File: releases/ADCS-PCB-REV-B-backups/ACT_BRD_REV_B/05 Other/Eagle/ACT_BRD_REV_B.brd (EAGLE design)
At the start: 91 x 91 mm, 228 parts, among them J11 TE_1-84953-1, J2 TE_1-84953-1, J4 TE_1-84953-1, J5 830-10-003-20-005000, U1 SIP2100DY-T1-GE3, U10 LM2917MX/NOPB, U12 TSV991AILT, U13 LM2917MX/NOPB, U14 ADS7841E_2K5, U16 DRV10970_MOTOR_DRIVERDRV10970, U17 LM2917MX/NOPB, U19 TSV991AILT, U2 SIP2100DY-T1-GE3, U20 ADS7841E_2K5, U3 SIP2100DY-T1-GE3, U6 DRV10970_MOTOR_DRIVERDRV10970, U7 DRV10970_MOTOR_DRIVERDRV10970, U8 TSV991AILT, U9 ADS7841E_2K5

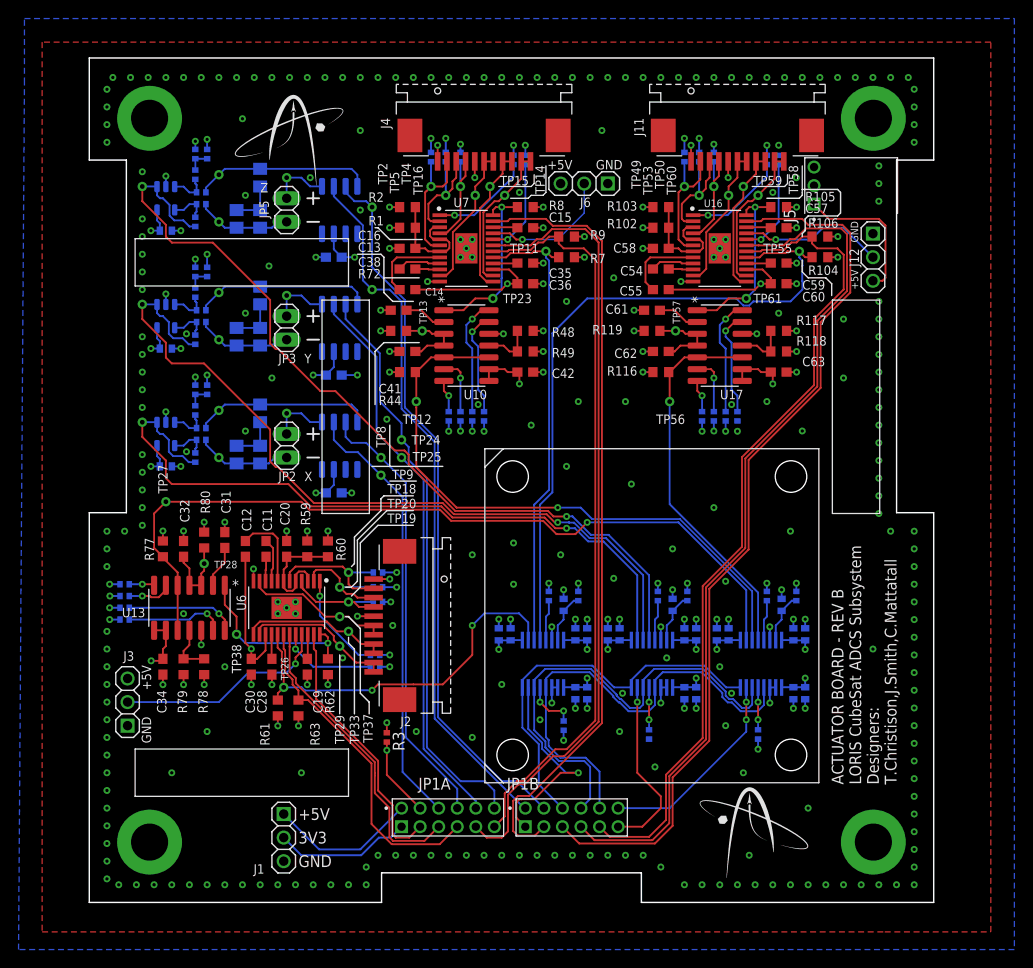
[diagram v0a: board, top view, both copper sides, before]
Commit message: Finalized connectors for Luc and reattached burn wire
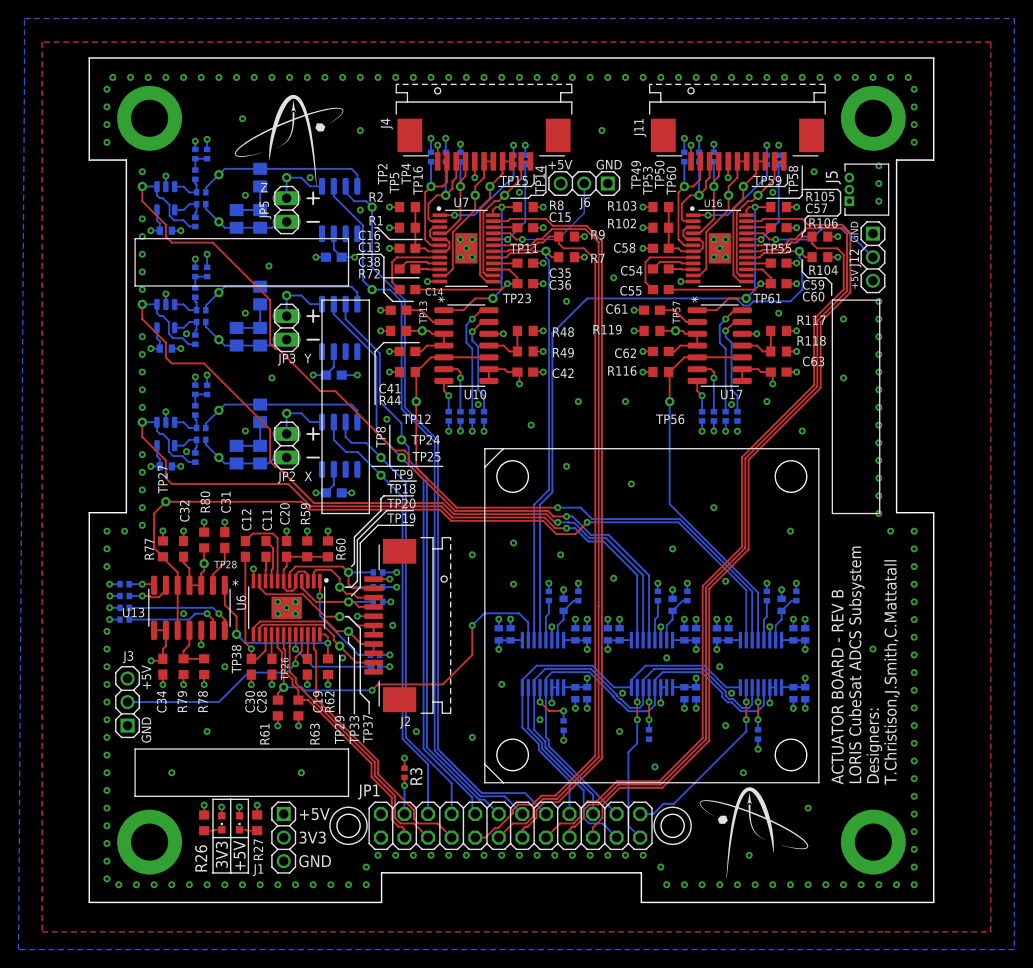
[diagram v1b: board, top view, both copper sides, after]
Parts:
- removed JP1A, JP1B: 832-10-012-10-005000, 832-10-012-10-005000:832-10-012-10-005000
- added JP1: (no value), pinhead:2X12
- added LED1, LED2: (no value), led:CHIPLED_0603
- added R26, R27: 470R, rcl:R0603
- J5: value 830-10-003-20-005000 -> TE-1734829-3; device 830-10-003-20-005000:830-10-003-20-005000 -> my_library:TE-1734829-3
- R22, R42, R88: value 470R -> DNP
- moved R3 4.26 mm to (34.0, 14.0)
- moved J5 3.82 mm to (81.9, 75.6), turned to 270 degrees
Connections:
- new net N$14: LED2.C, R27.2
- new net N$5: LED1.C, R26.2
- net !CS!_CURR_SENSE_MTQR: now also JP1.23; no longer JP1B.11
- net !CS!_CURR_SENSE_RW: now also JP1.21; no longer JP1B.1
- net !CS!_SPD_SENSE_RW: now also JP1.24; no longer JP1B.12
- net +3V3: now also JP1.1, LED2.A; no longer JP1A.1
- net +5V: now also JP1.2, LED1.A; no longer JP1A.2
- net GND: now also R26.1, R27.1
- net MAG_X_FIN: now also JP1.8; no longer JP1A.8
- net MAG_X_RIN: now also JP1.6; no longer JP1A.6
- net MAG_Y_FIN: now also JP1.12; no longer JP1A.12
- net MAG_Y_RIN: now also JP1.10; no longer JP1A.10
- net MAG_Z_FIN: now also JP1.16; no longer JP1B.4
- net MAG_Z_RIN: now also JP1.14; no longer JP1B.2
- net N$1: now also JP1.4; no longer JP1A.4
- net RW_X_DIR: now also JP1.13; no longer JP1B.3
- net RW_X_LOCK: now also JP1.9; no longer JP1A.11
- net RW_X_SPEED_CTRL: now also JP1.11; no longer JP1A.9
- net RW_Y_DIR: now also JP1.19; no longer JP1B.5
- net RW_Y_LOCK: now also JP1.15; no longer JP1B.9
- net RW_Y_SPEED_CTRL: now also JP1.17; no longer JP1B.7
- net RW_Z_DIR: now also JP1.7; no longer JP1A.3
- net RW_Z_LOCK: now also JP1.3; no longer JP1A.7
- net RW_Z_SPEED_CTRL: now also JP1.5; no longer JP1A.5
- net UCB0_SPI_CLK: now also JP1.18; no longer JP1B.6
- net UCB0_SPI_MISO: now also JP1.22; no longer JP1B.10
- net UCB0_SPI_MOSI: now also JP1.20; no longer JP1B.8
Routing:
- net +5V: track 122.8 -> 91.9 mm, vias 27 -> 28
- net +3V3: track 76.8 -> 63.0 mm, vias 24 -> 25
- net RW_Z_LOCK: track 35.9 -> 28.1 mm
- net RW_Y_DIR: track 97.2 -> 91.3 mm
- net N$1: track 8.61 -> 3.95 mm
- net RW_X_LOCK: track 79.9 -> 83.4 mm
- net RW_Z_SPEED_CTRL: track 32.4 -> 28.9 mm
- net RW_X_DIR: track 85.0 -> 81.7 mm
- net RW_Y_LOCK: track 89.6 -> 92.6 mm
- net RW_X_SPEED_CTRL: track 85.6 -> 83.0 mm
- net MAG_Z_FIN: track 77.5 -> 80.1 mm
- net !CS!_CURR_SENSE_MTQR: track 19.5 -> 17.1 mm, vias 1 -> 2
- net !CS!_CURR_SENSE_RW: track 23.2 -> 21.0 mm, vias 1 -> 0
- net !CS!_SPD_SENSE_RW: track 22.0 -> 19.9 mm
- net GND: track 120.9 -> 123.0 mm, vias 356 -> 359
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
